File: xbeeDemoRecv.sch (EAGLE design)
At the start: 11 parts, among them M1 9g

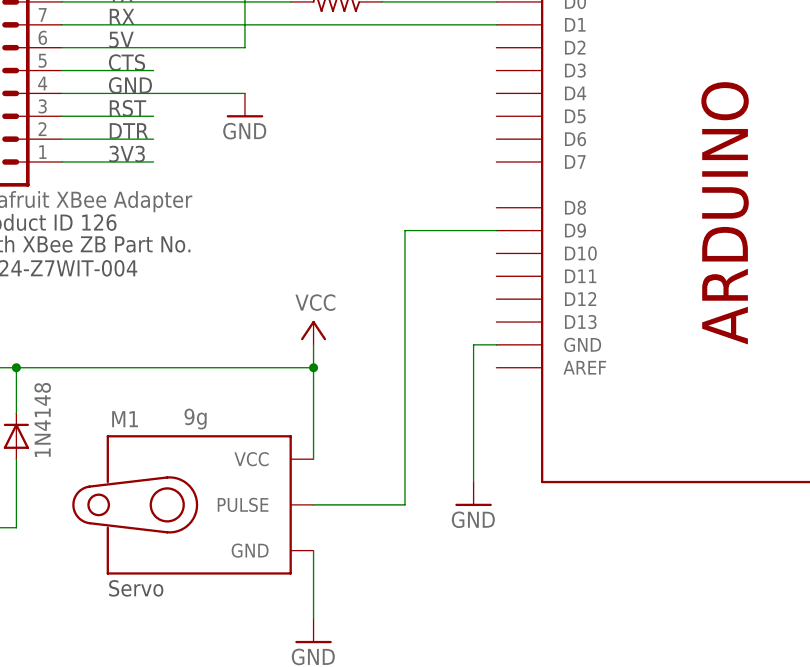
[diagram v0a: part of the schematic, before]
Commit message: Ground pin 7 for receiver.
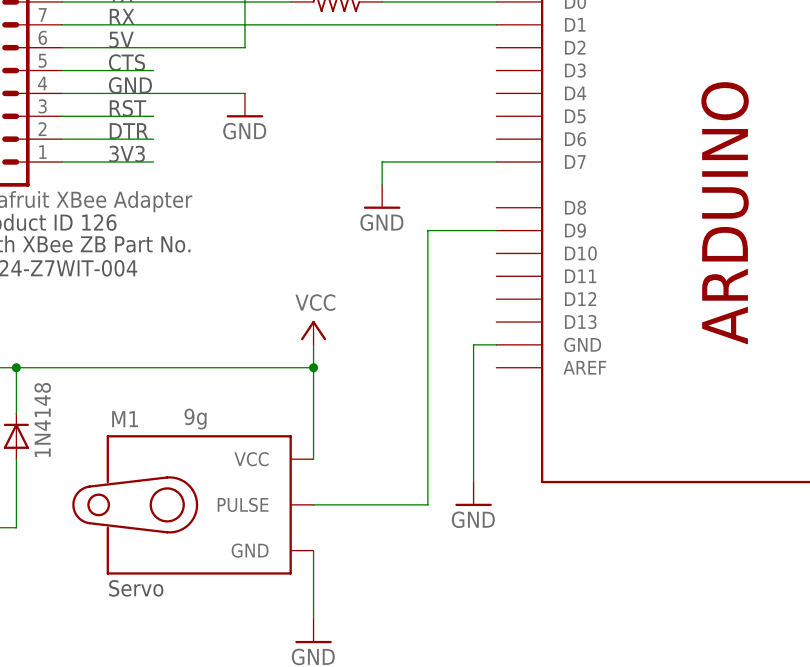
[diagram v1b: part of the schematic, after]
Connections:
- net GND: now also U$1.D7
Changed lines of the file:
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@@
 <part name="D3" library="_jc" deviceset="DIODE" device="1N4148" value="1N4148"/>
 <part name="GND4" library="supply1" deviceset="GND" device=""/>
+<part name="GND5" library="supply1" deviceset="GND" device=""/>
 </parts>
 <sheets>
@@
 <attribute name="VALUE" x="60.96" y="73.66" size="1.778" layer="96"/>
 </instance>
+<instance part="GND5" gate="1" x="116.84" y="116.84" smashed="yes">
+<attribute name="VALUE" x="114.3" y="114.3" size="1.778" layer="96"/>
+</instance>
 </instances>
 <busses>
@@
 <pinref part="GND4" gate="1" pin="GND"/>
 </segment>
+<segment>
+<pinref part="U$1" gate="G$1" pin="D7"/>
+<wire x1="129.54" y1="121.92" x2="116.84" y2="121.92" width="0.1524" layer="91"/>
+<wire x1="116.84" y1="121.92" x2="116.84" y2="119.38" width="0.1524" layer="91"/>
+<pinref part="GND5" gate="1" pin="GND"/>
+</segment>
 </net>
 <net name="N$1" class="0">
@@
 <segment>
 <pinref part="U$1" gate="G$1" pin="D9"/>
-<wire x1="129.54" y1="114.3" x2="119.38" y2="114.3" width="0.1524" layer="91"/>
+<wire x1="129.54" y1="114.3" x2="121.92" y2="114.3" width="0.1524" layer="91"/>
 <pinref part="M1" gate="G$1" pin="PULSE"/>
-<wire x1="109.22" y1="83.82" x2="119.38" y2="83.82" width="0.1524" layer="91"/>
-<wire x1="119.38" y1="83.82" x2="119.38" y2="114.3" width="0.1524" layer="91"/>
-</segment>
-</net>
+<wire x1="109.22" y1="83.82" x2="121.92" y2="83.82" width="0.1524" layer="91"/>
+<wire x1="121.92" y1="83.82" x2="121.92" y2="114.3" width="0.1524" layer="91"/>
+</segment>
+</net>
